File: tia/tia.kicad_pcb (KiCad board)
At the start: 4 copper layers, 63.5 x 37.5 mm, 29 parts, among them J1 ToADC, J2 Sensors, U1 Opamp_Quad, U2 Opamp_Quad, U3 MIC5366-2.0YC5-TR

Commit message: board revs, updated README
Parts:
- added C10: 10pF, Capacitor_SMD:C_0805_2012Metric, F.Cu at (138.0, 123.0)
- added C11: 10pF, Capacitor_SMD:C_0805_2012Metric, F.Cu at (138.0, 105.5)
- added C12: 10pF, Capacitor_SMD:C_0805_2012Metric, F.Cu at (138.0, 108.8)
- added C13: 10pF, Capacitor_SMD:C_0805_2012Metric, F.Cu at (138.0, 91.5)
- added C14: 10pF, Capacitor_SMD:C_0805_2012Metric, F.Cu at (133.2, 108.8)
- added C15: 10pF, Capacitor_SMD:C_0805_2012Metric, F.Cu at (133.2, 91.5)
- added C7: 0.01uF X7R, Capacitor_SMD:C_0805_2012Metric, F.Cu at (101.6, 90.4)
- added C8: 10pF, Capacitor_SMD:C_0805_2012Metric, F.Cu at (133.2, 123.0)
- added C9: 10pF, Capacitor_SMD:C_0805_2012Metric, F.Cu at (133.2, 105.5)
- moved C3 1.20 mm to (97.8, 89.5)
- moved R3 1.13 mm to (138.0, 110.8)
- moved R4 1.12 mm to (133.2, 110.8)
- moved R5 1.07 mm to (133.2, 103.5)
- moved R6 1.07 mm to (138.0, 103.5)
- moved C4 0.50 mm to (131.5, 115.8)
- moved C5 0.50 mm to (131.5, 98.2)
- moved U1 0.50 mm to (135.6, 115.9)
- moved U2 0.50 mm to (135.6, 98.5)
- moved R2 0.26 mm to (138.0, 120.9)
- moved R1 0.25 mm to (133.2, 120.9)
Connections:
- J1 pad 1: /VREF -> /A0N
- J1 pad 10: /A4N -> /VREF
- J1 pad 11: /VREF -> /A5N
- J1 pad 12: /A5N -> /VREF
- J1 pad 13: /VREF -> /A6N
- J1 pad 14: /A6N -> /VREF
- J1 pad 15: /VREF -> /A7N
- J1 pad 16: /A7N -> /VREF
- J1 pad 17: GND -> /VREF
- J1 pad 18: /VREF -> GND
- J1 pad 19: GND -> VAA
- J1 pad 2: /A0N -> /VREF
- J1 pad 20: VAA -> GND
- J1 pad 3: /VREF -> /A1N
- J1 pad 4: /A1N -> /VREF
- J1 pad 5: /VREF -> /A2N
- J1 pad 6: /A2N -> /VREF
- J1 pad 7: /VREF -> /A3N
- J1 pad 8: /A3N -> /VREF
- J1 pad 9: /VREF -> /A4N
- U3 pad 4: unconnected-(U3-BYP-Pad4) -> Net-(U3-BYP)
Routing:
- net /VREF: track 96.9 -> 117.2 mm
- net VAA: track 12.6 -> 20.2 mm
- net /A7N: track 40.9 -> 45.9 mm
- net /A5N: track 46.3 -> 51.1 mm
- net /A3N: track 38.9 -> 43.6 mm
- net Net-(U3-BYP): track 0.00 -> 4.70 mm
- net /A0N: track 40.5 -> 44.7 mm
- net /A1N: track 50.5 -> 54.5 mm
- net /A2N: track 51.7 -> 55.8 mm
- net /A4N: track 46.5 -> 50.3 mm
- net /A6N: track 54.3 -> 57.3 mm
- net /S0: track 19.7 -> 22.1 mm
- net /S6: track 15.4 -> 17.4 mm
- net /S7: track 19.0 -> 21.0 mm
- net /S4: track 16.5 -> 18.3 mm
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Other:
- board text added: "Simple TIA Adapter rev1"
- board text removed: "Simple TIA Adapter rev0"

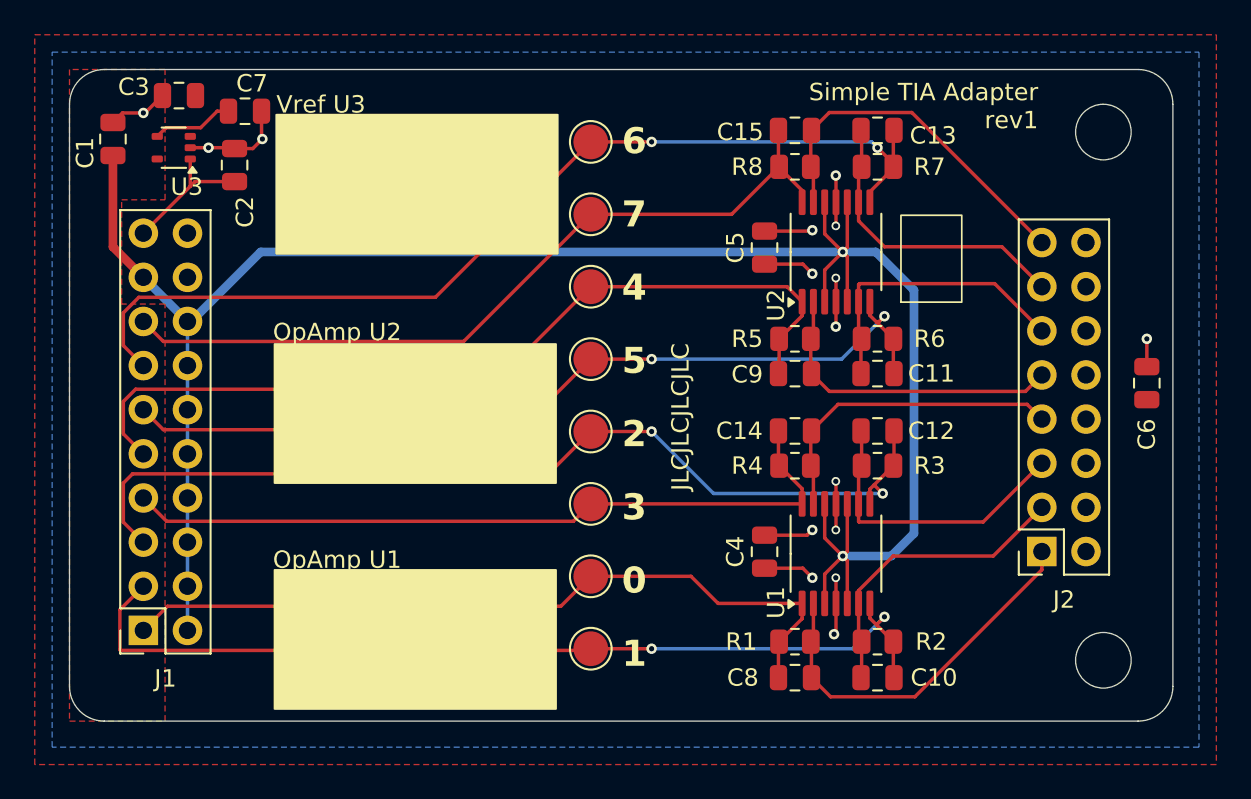
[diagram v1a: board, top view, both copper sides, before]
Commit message: rev2 of tia board, with bias and LPF
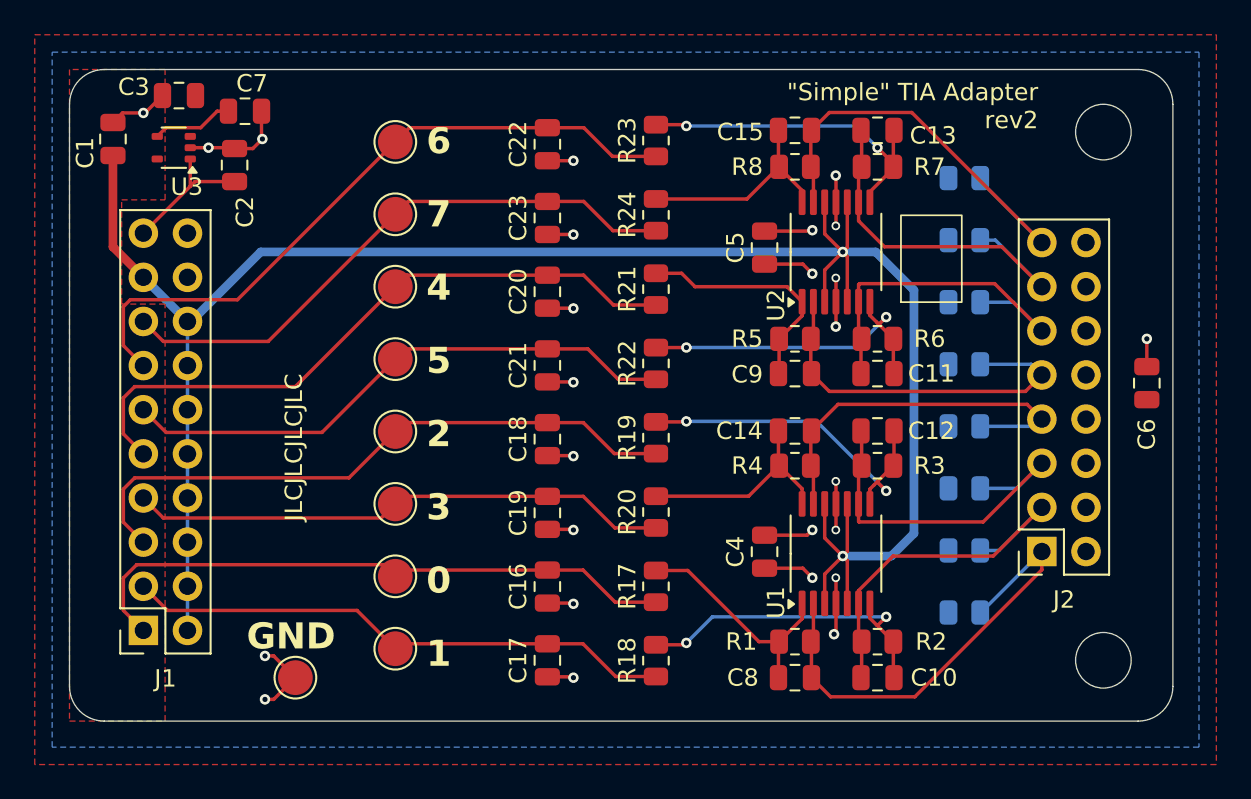
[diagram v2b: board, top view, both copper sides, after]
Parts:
- added C16: 10nF, Capacitor_SMD:C_0805_2012Metric, F.Cu at (119.0, 117.8)
- added C17: 10nF, Capacitor_SMD:C_0805_2012Metric, F.Cu at (119.0, 122.0)
- added C18: 10nF, Capacitor_SMD:C_0805_2012Metric, F.Cu at (119.0, 109.3)
- added C19: 10nF, Capacitor_SMD:C_0805_2012Metric, F.Cu at (119.0, 113.5)
- added C20: 10nF, Capacitor_SMD:C_0805_2012Metric, F.Cu at (119.0, 100.8)
- added C21: 10nF, Capacitor_SMD:C_0805_2012Metric, F.Cu at (119.0, 105.0)
- added C22: 10nF, Capacitor_SMD:C_0805_2012Metric, F.Cu at (119.0, 92.3)
- added C23: 10nF, Capacitor_SMD:C_0805_2012Metric, F.Cu at (119.0, 96.5)
- added R10: 500k, Resistor_SMD:R_0805_2012Metric, B.Cu at (143.0, 115.7)
- added R11: 500k, Resistor_SMD:R_0805_2012Metric, B.Cu at (143.0, 112.1)
- added R12: 500k, Resistor_SMD:R_0805_2012Metric, B.Cu at (143.0, 108.5)
- added R13: 500k, Resistor_SMD:R_0805_2012Metric, B.Cu at (143.0, 105.0)
- added R14: 500k, Resistor_SMD:R_0805_2012Metric, B.Cu at (143.0, 101.4)
- added R15: 500k, Resistor_SMD:R_0805_2012Metric, B.Cu at (143.0, 97.8)
- added R16: 500k, Resistor_SMD:R_0805_2012Metric, B.Cu at (143.0, 94.2)
- added R17: 1000, Resistor_SMD:R_0805_2012Metric, F.Cu at (125.2, 117.7)
- added R18: 1000, Resistor_SMD:R_0805_2012Metric, F.Cu at (125.2, 122.0)
- added R19: 1000, Resistor_SMD:R_0805_2012Metric, F.Cu at (125.2, 109.2)
- added R20: 1000, Resistor_SMD:R_0805_2012Metric, F.Cu at (125.2, 113.5)
- added R21: 1000, Resistor_SMD:R_0805_2012Metric, F.Cu at (125.2, 100.6)
- added R22: 1000, Resistor_SMD:R_0805_2012Metric, F.Cu at (125.2, 104.9)
- added R23: 1000, Resistor_SMD:R_0805_2012Metric, F.Cu at (125.2, 92.1)
- added R24: 1000, Resistor_SMD:R_0805_2012Metric, F.Cu at (125.2, 96.4)
- added R9: 500k, Resistor_SMD:R_0805_2012Metric, B.Cu at (143.0, 119.2)
- added TP9: TestPoint, TestPoint:TestPoint_Pad_D2.0mm, F.Cu at (104.5, 123.0)
- C10, C11, C12, C13, C14, C15, C8, C9: value 10pF -> 10nF
- R1, R2, R3, R4, R5, R6, R7, R8: value 1000 -> 2870
- moved TP1 11.2 mm to (110.2, 117.2)
- moved TP2 11.2 mm to (110.2, 121.3)
- moved TP3 11.2 mm to (110.2, 108.8)
- moved TP4 11.2 mm to (110.2, 113.0)
- moved TP5 11.2 mm to (110.2, 100.5)
- moved TP6 11.2 mm to (110.2, 104.7)
- moved TP7 11.2 mm to (110.2, 92.2)
- moved TP8 11.2 mm to (110.2, 96.3)
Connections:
- C10 pad 2: /A1N -> Net-(C10-Pad2)
- C11 pad 2: /A5N -> Net-(C11-Pad2)
- C12 pad 2: /A2N -> Net-(C12-Pad2)
- C13 pad 2: /A6N -> Net-(C13-Pad2)
- C14 pad 2: /A3N -> Net-(C14-Pad2)
- C15 pad 2: /A7N -> Net-(C15-Pad2)
- C8 pad 2: /A0N -> Net-(C8-Pad2)
- C9 pad 2: /A4N -> Net-(C9-Pad2)
- R1 pad 2: /A0N -> Net-(C8-Pad2)
- R2 pad 2: /A1N -> Net-(C10-Pad2)
- R3 pad 2: /A2N -> Net-(C12-Pad2)
- R4 pad 2: /A3N -> Net-(C14-Pad2)
- R5 pad 2: /A4N -> Net-(C9-Pad2)
- R6 pad 2: /A5N -> Net-(C11-Pad2)
- R7 pad 2: /A6N -> Net-(C13-Pad2)
- R8 pad 2: /A7N -> Net-(C15-Pad2)
- U1 pad 1: /A0N -> Net-(C8-Pad2)
- U1 pad 14: /A3N -> Net-(C14-Pad2)
- U1 pad 7: /A1N -> Net-(C10-Pad2)
- U1 pad 8: /A2N -> Net-(C12-Pad2)
- U2 pad 1: /A4N -> Net-(C9-Pad2)
- U2 pad 14: /A7N -> Net-(C15-Pad2)
- U2 pad 7: /A5N -> Net-(C11-Pad2)
- U2 pad 8: /A6N -> Net-(C13-Pad2)
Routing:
- net /A1N: track 54.5 -> 31.9 mm, vias 2 -> 0
- net Net-(C12-Pad2): track 0.00 -> 20.4 mm, vias 0 -> 2
- net Net-(C11-Pad2): track 0.00 -> 19.7 mm, vias 0 -> 2
- net Net-(C10-Pad2): track 0.00 -> 19.5 mm, vias 0 -> 2
- net Net-(C13-Pad2): track 0.00 -> 19.5 mm, vias 0 -> 2
- net /A2N: track 55.8 -> 36.5 mm, vias 2 -> 0
- net /A5N: track 51.1 -> 32.8 mm, vias 2 -> 0
- net /A6N: track 57.3 -> 39.5 mm, vias 2 -> 0
- net GND: track 22.6 -> 39.2 mm, vias 10 -> 20
- net Net-(C9-Pad2): track 0.00 -> 13.8 mm
- net Net-(C8-Pad2): track 0.00 -> 13.6 mm
- net Net-(C14-Pad2): track 0.00 -> 12.6 mm
- net Net-(C15-Pad2): track 0.00 -> 12.6 mm
- net /A3N: track 43.6 -> 31.2 mm
- net /A4N: track 50.3 -> 38.0 mm
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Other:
- board text added: "GND"
- board text added: "{dblquote}Simple{dblquote} TIA Adapter rev2"
- board text removed: "OpAmp U1"
- board text removed: "OpAmp U2"
- board text removed: "Simple TIA Adapter rev1"
- board text removed: "Vref U3"
